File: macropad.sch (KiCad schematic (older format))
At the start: 47 parts, among them P1 USB_C_Plug_USB2.0, SW1 SW_Push, SW10 SW_Push, SW11 Rotary_Encoder_Switch, SW2 SW_Push, SW3 SW_Push, SW4 Rotary_Encoder_Switch, SW5 SW_Push, SW6 SW_Push, SW7 SW_Push, SW8 SW_Push, SW9 SW_Push, U1 ATmega16U2-MU, Y1 16MHz

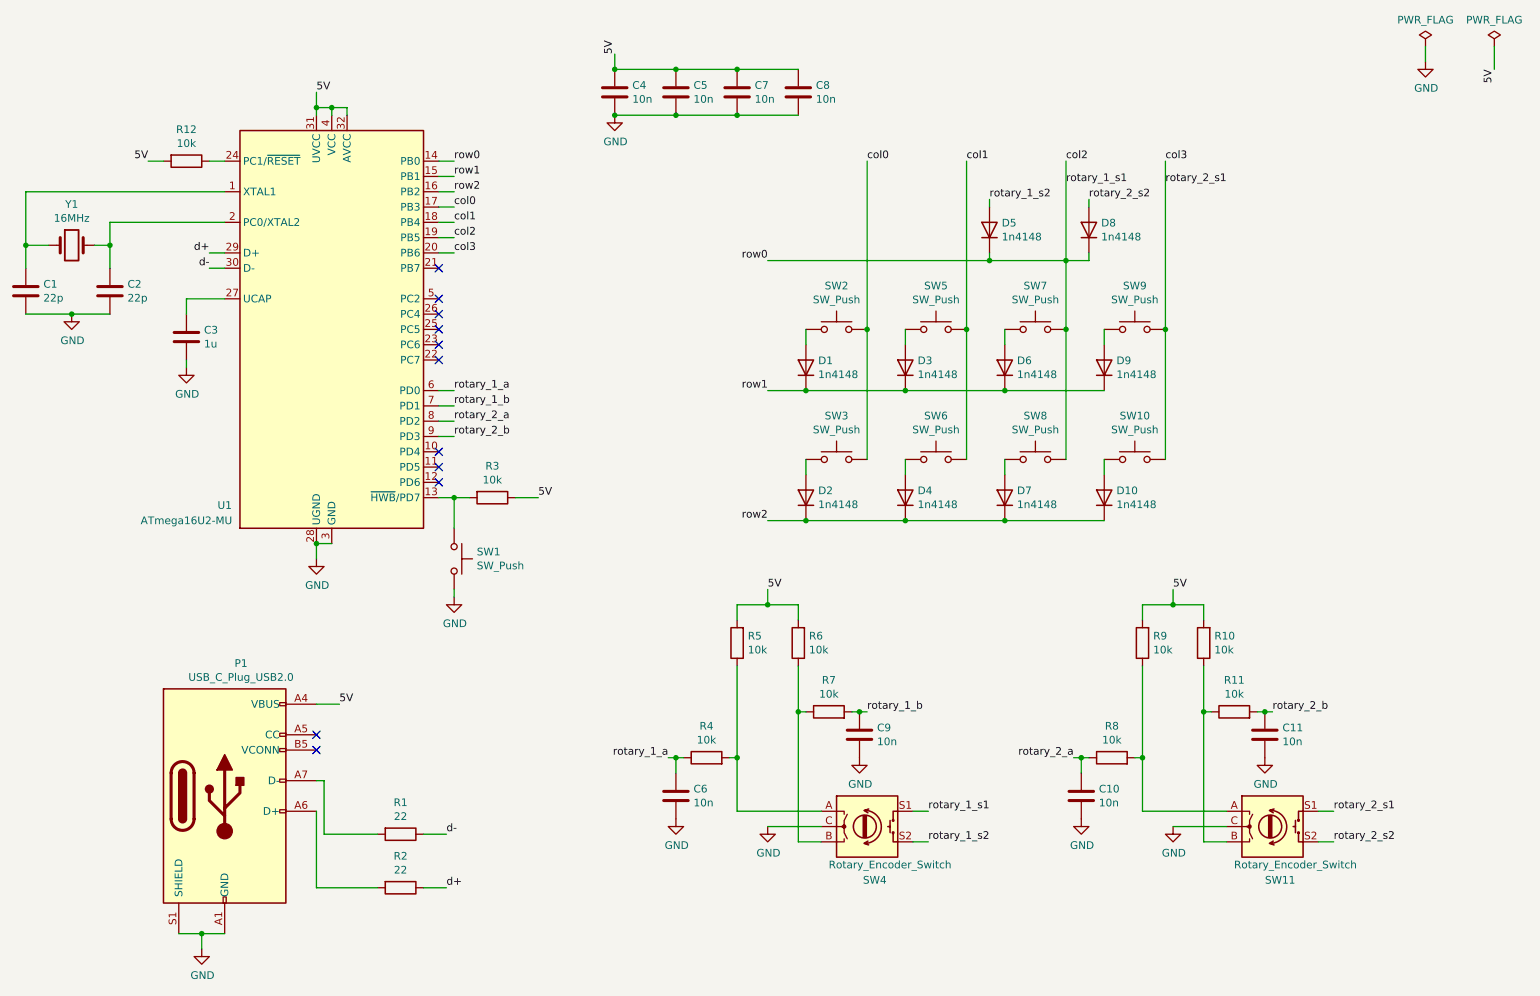
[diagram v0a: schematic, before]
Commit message: use actual models
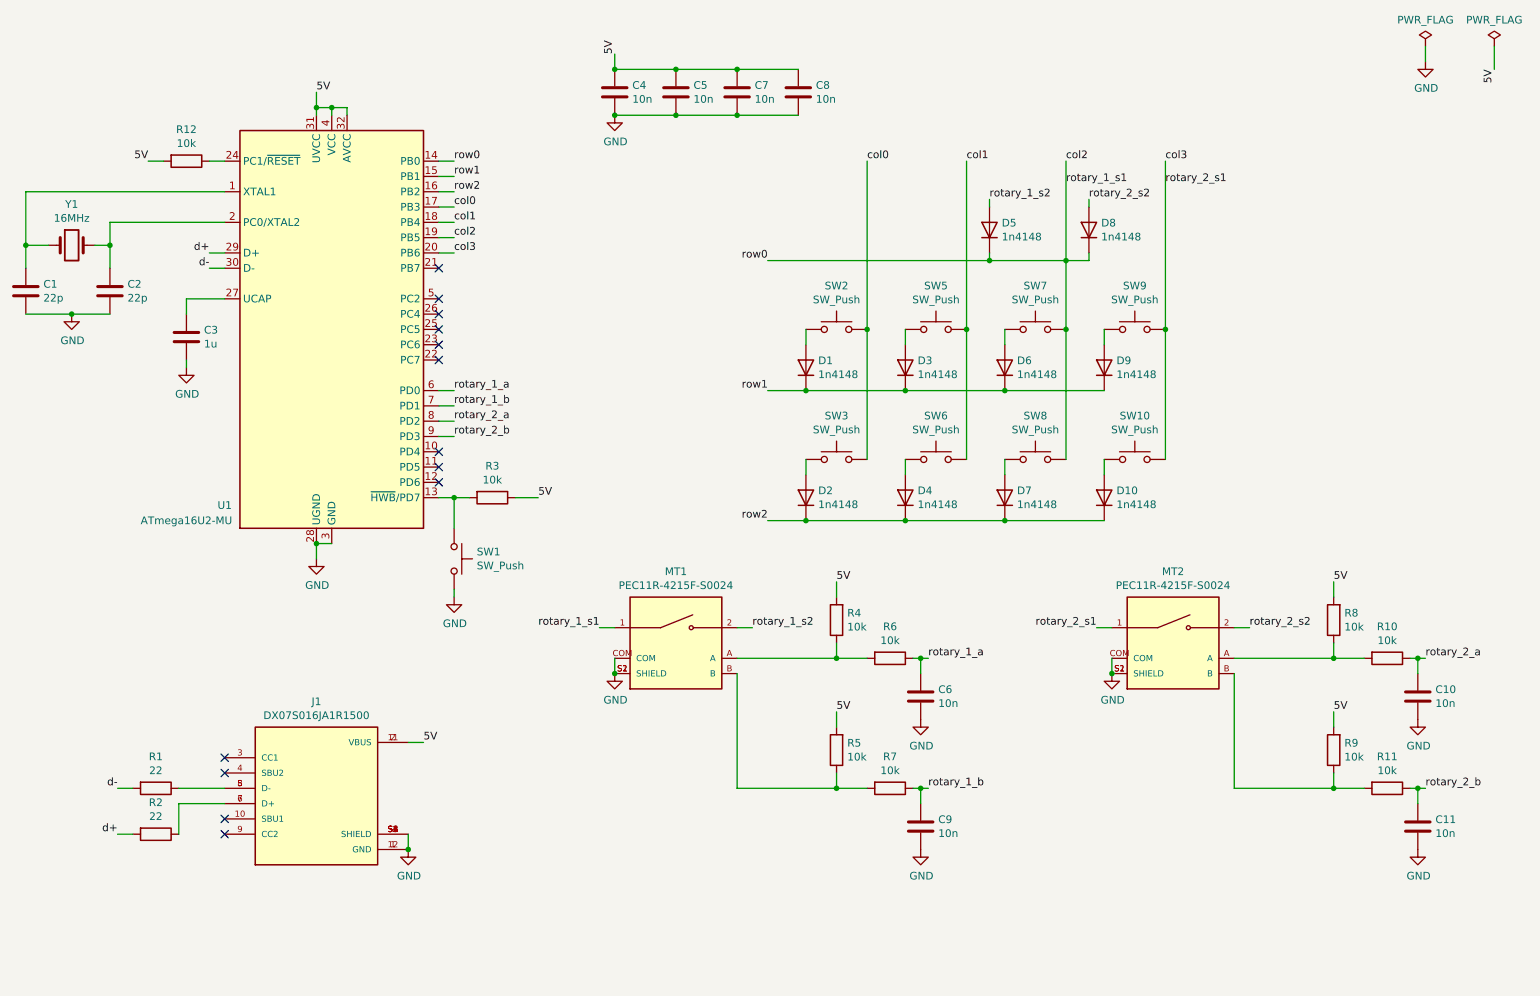
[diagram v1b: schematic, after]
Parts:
- removed P1: USB_C_Plug_USB2.0, DX07S016JA1R1500:JAE_DX07S016JA1R1500, symbol Connector:USB_C_Plug_USB2.0
- removed SW11, SW4: Rotary_Encoder_Switch, PEC11R-4215F-S0024:XDCR_PEC11R-4215F-S0024, symbol Device:Rotary_Encoder_Switch
- added J1: DX07S016JA1R1500, DX07S016JA1R1500:JAE_DX07S016JA1R1500, symbol DX07S016JA1R1500:DX07S016JA1R1500
- added MT1, MT2: PEC11R-4215F-S0024, PEC11R-4215F-S0024:XDCR_PEC11R-4215F-S0024, symbol PEC11R-4215F-S0024:PEC11R-4215F-S0024
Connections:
- net 5V: now also R4.2, R8.2, J1.11 (VBUS), J1.2 (VBUS); no longer R10.2, R6.2
- net GND: now also J1.1 (GND), J1.12 (GND), J1.S1 (SHIELD), J1.S2 (SHIELD), J1.S3 (SHIELD), J1.S4 (SHIELD), J1.S5 (SHIELD), J1.S6 (SHIELD), MT1.COM, MT1.S1 (SHIELD), MT1.S2 (SHIELD), MT2.COM, MT2.S1 (SHIELD), MT2.S2 (SHIELD)
- net col2: now also MT1.1
- net col3: now also MT2.1
- net d+: now also R2.2; no longer R2.1
- net d-: now also R1.2; no longer R1.1
- net rotary_1_a: now also R6.1; no longer R4.1
- net rotary_1_b: now also R7.1; no longer R7.2
- net rotary_1_s2: now also MT1.2
- net rotary_2_a: now also R10.1; no longer R8.1
- net rotary_2_b: now also R11.1; no longer R11.2
- net rotary_2_s2: now also MT2.2
- net at R5.1: now also R7.2, MT1.B; no longer R4.2
- net at R9.1: now also R11.2, MT2.B; no longer R8.2
- new net: J1.5 (D-), J1.8 (D-), R1.1
- new net: J1.6 (D+), J1.7 (D+), R2.1
- new net: MT1.A, R4.1, R6.2
- new net: MT2.A, R10.2, R8.1
- no-connect marks 11 -> 13

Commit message: seems like a good place to leave it for today
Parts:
- removed C8: 10n, Capacitor_SMD:C_0603_1608Metric, symbol Device:C
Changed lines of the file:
@@
-	1    0    0    -1
-$EndComp
-$Comp
-L Device:C C8
-U 1 1 6056B643
-P 6100 1150
-F 0 "C8" H 6215 1196 50  0000 L CNN
-F 1 "10n" H 6215 1105 50  0000 L CNN
-F 2 "Capacitor_SMD:C_0603_1608Metric" H 6138 1000 50  0001 C CNN
-F 3 "~" H 6100 1150 50  0001 C CNN
-	1    6100 1150
 	1    0    0    -1
 $EndComp
@@
 Connection ~ 5300 1300
 Wire Wire Line
-	5700 1300 6100 1300
-Connection ~ 5700 1300
-Wire Wire Line
-	6100 1000 5700 1000
-Wire Wire Line
 	5700 1000 5300 1000
-Connection ~ 5700 1000
 Wire Wire Line
 	4900 1000 5300 1000

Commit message: Fix everything forever
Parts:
- removed Y1: 16MHz, Crystal:Crystal_SMD_3225-4Pin_3.2x2.5mm, symbol Device:Crystal
- added Y1: 16MHz, Crystal:Crystal_SMD_3225-4Pin_3.2x2.5mm, symbol Device:Crystal_GND24
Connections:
- net GND: now also Y1.2, Y1.4
- net at C1.1, U1.1 (XTAL1): now also Y1.1
- net at C2.1, U1.2 (PC0/XTAL2): now also Y1.3
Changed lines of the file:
@@
 	2250 1600 2350 1600
-$Comp
-L Device:Crystal Y1
-U 1 1 60533B4C
-P 1350 2150
-F 0 "Y1" H 1350 2418 50  0000 C CNN
-F 1 "16MHz" H 1350 2327 50  0000 C CNN
-F 2 "Crystal:Crystal_SMD_3225-4Pin_3.2x2.5mm" H 1350 2150 50  0001 C CNN
-F 3 "~" H 1350 2150 50  0001 C CNN
-	1    1350 2150
-	1    0    0    -1
-$EndComp
 $Comp
 L Device:C C1
@@
 	8950 5700 9600 5700
 Connection ~ 9600 5700
+$Comp
+L Device:Crystal_GND24 Y1
+U 1 1 6050F71C
+P 1350 2150
+F 0 "Y1" H 1544 2196 50  0000 L CNN
+F 1 "16MHz" H 1544 2105 50  0000 L CNN
+F 2 "Crystal:Crystal_SMD_3225-4Pin_3.2x2.5mm" H 1350 2150 50  0001 C CNN
+F 3 "~" H 1350 2150 50  0001 C CNN
+	1    1350 2150
+	1    0    0    -1
+$EndComp
+Wire Wire Line
+	1350 2350 1350 2450
+Wire Wire Line
+	1350 1950 1150 1950
+Wire Wire Line
+	1150 1950 1150 2450
+Wire Wire Line
+	1150 2450 1350 2450
+Connection ~ 1350 2450
+Wire Wire Line
+	1350 2450 1350 2600
 $EndSCHEMATC

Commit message: missed a spot
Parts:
- C1, C2: LCSC (none) -> C1653
- C10, C11, C4, C5, C6, C7, C9: LCSC (none) -> C57112
- C3: LCSC (none) -> C15849
- D1, D10, D2, D3, D4, D5, D6, D7, D8, D9: LCSC (none) -> C2128
- R1, R2: LCSC (none) -> C23345
- R10, R11, R12, R3, R4, R5, R6, R7, R8, R9: LCSC (none) -> C25804
- U1: LCSC (none) -> C17317
- Y1: LCSC (none) -> C13738
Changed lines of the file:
@@
 F 2 "Package_DFN_QFN:QFN-32-1EP_5x5mm_P0.5mm_EP3.1x3.1mm" H 3050 2700 50  0001 C CIN
 F 3 "http://ww1.microchip.com/downloads/en/DeviceDoc/doc7799.pdf" H 3050 2700 50  0001 C CNN
+F 4 "C17317" H 3050 2700 50  0001 C CNN "LCSC"
 	1    3050 2700
 	1    0    0    -1
@@
 F 2 "Diode_SMD:D_SOD-323F" H 6150 2950 50  0001 C CNN
 F 3 "~" H 6150 2950 50  0001 C CNN
+F 4 "C2128" V 6150 2950 50  0001 C CNN "LCSC"
 	1    6150 2950
 	0    -1   -1   0
@@
 F 2 "Diode_SMD:D_SOD-323F" H 6800 2950 50  0001 C CNN
 F 3 "~" H 6800 2950 50  0001 C CNN
+F 4 "C2128" V 6800 2950 50  0001 C CNN "LCSC"
 	1    6800 2950
 	0    -1   -1   0
@@
 F 2 "Diode_SMD:D_SOD-323F" H 7450 2950 50  0001 C CNN
 F 3 "~" H 7450 2950 50  0001 C CNN
+F 4 "C2128" V 7450 2950 50  0001 C CNN "LCSC"
 	1    7450 2950
 	0    -1   -1   0
@@
 F 2 "Diode_SMD:D_SOD-323F" H 8100 2950 50  0001 C CNN
 F 3 "~" H 8100 2950 50  0001 C CNN
+F 4 "C2128" V 8100 2950 50  0001 C CNN "LCSC"
 	1    8100 2950
 	0    -1   -1   0
@@
 F 2 "Diode_SMD:D_SOD-323F" H 6150 3800 50  0001 C CNN
 F 3 "~" H 6150 3800 50  0001 C CNN
+F 4 "C2128" V 6150 3800 50  0001 C CNN "LCSC"
 	1    6150 3800
 	0    -1   -1   0
@@
 F 2 "Diode_SMD:D_SOD-323F" H 6800 3800 50  0001 C CNN
 F 3 "~" H 6800 3800 50  0001 C CNN
+F 4 "C2128" V 6800 3800 50  0001 C CNN "LCSC"
 	1    6800 3800
 	0    -1   -1   0
@@
 F 2 "Diode_SMD:D_SOD-323F" H 7450 3800 50  0001 C CNN
 F 3 "~" H 7450 3800 50  0001 C CNN
+F 4 "C2128" V 7450 3800 50  0001 C CNN "LCSC"
 	1    7450 3800
 	0    -1   -1   0
@@
 F 2 "Diode_SMD:D_SOD-323F" H 8100 3800 50  0001 C CNN
 F 3 "~" H 8100 3800 50  0001 C CNN
+F 4 "C2128" V 8100 3800 50  0001 C CNN "LCSC"
 	1    8100 3800
 	0    -1   -1   0
@@
 F 2 "Diode_SMD:D_SOD-323F" H 7350 2050 50  0001 C CNN
 F 3 "~" H 7350 2050 50  0001 C CNN
+F 4 "C2128" V 7350 2050 50  0001 C CNN "LCSC"
 	1    7350 2050
 	0    -1   -1   0
@@
 F 2 "Diode_SMD:D_SOD-323F" H 8000 2050 50  0001 C CNN
 F 3 "~" H 8000 2050 50  0001 C CNN
+F 4 "C2128" V 8000 2050 50  0001 C CNN "LCSC"
 	1    8000 2050
 	0    -1   -1   0
@@
 F 2 "Capacitor_SMD:C_0603_1608Metric" H 2138 2600 50  0001 C CNN
 F 3 "~" H 2100 2750 50  0001 C CNN
+F 4 "C15849" H 2100 2750 50  0001 C CNN "LCSC"
 	1    2100 2750
 	1    0    0    -1
@@
 F 2 "Capacitor_SMD:C_0603_1608Metric" H 1088 2300 50  0001 C CNN
 F 3 "~" H 1050 2450 50  0001 C CNN
+F 4 "C1653" H 1050 2450 50  0001 C CNN "LCSC"
 	1    1050 2450
 	1    0    0    -1
@@
 F 2 "Capacitor_SMD:C_0603_1608Metric" H 1638 2300 50  0001 C CNN
 F 3 "~" H 1600 2450 50  0001 C CNN
+F 4 "C1653" H 1600 2450 50  0001 C CNN "LCSC"
 	1    1600 2450
 	1    0    0    -1
@@
 F 2 "Capacitor_SMD:C_0603_1608Metric" H 4938 1000 50  0001 C CNN
 F 3 "~" H 4900 1150 50  0001 C CNN
+F 4 "C57112" H 4900 1150 50  0001 C CNN "LCSC"
 	1    4900 1150
 	1    0    0    -1
@@
 F 2 "Capacitor_SMD:C_0603_1608Metric" H 5338 1000 50  0001 C CNN
 F 3 "~" H 5300 1150 50  0001 C CNN
+F 4 "C57112" H 5300 1150 50  0001 C CNN "LCSC"
 	1    5300 1150
 	1    0    0    -1
@@
 F 2 "Capacitor_SMD:C_0603_1608Metric" H 5738 1000 50  0001 C CNN
 F 3 "~" H 5700 1150 50  0001 C CNN
+F 4 "C57112" H 5700 1150 50  0001 C CNN "LCSC"
 	1    5700 1150
 	1    0    0    -1
@@
 F 2 "Resistor_SMD:R_0603_1608Metric" V 4030 3800 50  0001 C CNN
 F 3 "~" H 4100 3800 50  0001 C CNN
+F 4 "C25804" V 4100 3800 50  0001 C CNN "LCSC"
 	1    4100 3800
 	0    1    1    0
@@
 F 2 "Resistor_SMD:R_0603_1608Metric" V 2030 1600 50  0001 C CNN
 F 3 "~" H 2100 1600 50  0001 C CNN
+F 4 "C25804" V 2100 1600 50  0001 C CNN "LCSC"
 	1    2100 1600
 	0    1    1    0
@@
 F 2 "Resistor_SMD:R_0603_1608Metric" V 1830 5700 50  0001 C CNN
 F 3 "~" H 1900 5700 50  0001 C CNN
+F 4 "C23345" V 1900 5700 50  0001 C CNN "LCSC"
 	1    1900 5700
 	0    1    1    0
@@
 F 2 "Resistor_SMD:R_0603_1608Metric" V 1830 6000 50  0001 C CNN
 F 3 "~" H 1900 6000 50  0001 C CNN
+F 4 "C23345" V 1900 6000 50  0001 C CNN "LCSC"
 	1    1900 6000
 	0    1    1    0
@@
 F 2 "Resistor_SMD:R_0603_1608Metric" V 6630 4850 50  0001 C CNN
 F 3 "~" H 6700 4850 50  0001 C CNN
+F 4 "C25804" V 6700 4850 50  0001 C CNN "LCSC"
 	1    6700 4850
 	0    1    1    0
@@
 F 2 "Capacitor_SMD:C_0603_1608Metric" H 6938 4950 50  0001 C CNN
 F 3 "~" H 6900 5100 50  0001 C CNN
+F 4 "C57112" H 6900 5100 50  0001 C CNN "LCSC"
 	1    6900 5100
 	1    0    0    -1
@@
 F 2 "Resistor_SMD:R_0603_1608Metric" V 6280 4600 50  0001 C CNN
 F 3 "~" H 6350 4600 50  0001 C CNN
+F 4 "C25804" H 6350 4600 50  0001 C CNN "LCSC"
 	1    6350 4600
 	-1   0    0    1
@@
 F 2 "Resistor_SMD:R_0603_1608Metric" V 6630 5700 50  0001 C CNN
 F 3 "~" H 6700 5700 50  0001 C CNN
+F 4 "C25804" V 6700 5700 50  0001 C CNN "LCSC"
 	1    6700 5700
 	0    1    1    0
@@
 F 2 "Capacitor_SMD:C_0603_1608Metric" H 6938 5800 50  0001 C CNN
 F 3 "~" H 6900 5950 50  0001 C CNN
+F 4 "C57112" H 6900 5950 50  0001 C CNN "LCSC"
 	1    6900 5950
 	1    0    0    -1
@@
 F 2 "Resistor_SMD:R_0603_1608Metric" V 6280 5450 50  0001 C CNN
 F 3 "~" H 6350 5450 50  0001 C CNN
+F 4 "C25804" H 6350 5450 50  0001 C CNN "LCSC"
 	1    6350 5450
 	-1   0    0    1
@@
 F 2 "Resistor_SMD:R_0603_1608Metric" V 9880 4850 50  0001 C CNN
 F 3 "~" H 9950 4850 50  0001 C CNN
+F 4 "C25804" V 9950 4850 50  0001 C CNN "LCSC"
 	1    9950 4850
 	0    1    1    0
@@
 F 2 "Capacitor_SMD:C_0603_1608Metric" H 10188 4950 50  0001 C CNN
 F 3 "~" H 10150 5100 50  0001 C CNN
+F 4 "C57112" H 10150 5100 50  0001 C CNN "LCSC"
 	1    10150 5100
 	1    0    0    -1
@@
 F 2 "Resistor_SMD:R_0603_1608Metric" V 9530 4600 50  0001 C CNN
 F 3 "~" H 9600 4600 50  0001 C CNN
+F 4 "C25804" H 9600 4600 50  0001 C CNN "LCSC"
 	1    9600 4600
 	-1   0    0    1
@@
 F 2 "Resistor_SMD:R_0603_1608Metric" V 9880 5700 50  0001 C CNN
 F 3 "~" H 9950 5700 50  0001 C CNN
+F 4 "C25804" V 9950 5700 50  0001 C CNN "LCSC"
 	1    9950 5700
 	0    1    1    0
@@
 F 2 "Capacitor_SMD:C_0603_1608Metric" H 10188 5800 50  0001 C CNN
 F 3 "~" H 10150 5950 50  0001 C CNN
+F 4 "C57112" H 10150 5950 50  0001 C CNN "LCSC"
 	1    10150 5950
 	1    0    0    -1
@@
 F 2 "Resistor_SMD:R_0603_1608Metric" V 9530 5450 50  0001 C CNN
 F 3 "~" H 9600 5450 50  0001 C CNN
+F 4 "C25804" H 9600 5450 50  0001 C CNN "LCSC"
 	1    9600 5450
 	-1   0    0    1
@@
 F 2 "Crystal:Crystal_SMD_3225-4Pin_3.2x2.5mm" H 1350 2150 50  0001 C CNN
 F 3 "~" H 1350 2150 50  0001 C CNN
+F 4 "C13738" H 1350 2150 50  0001 C CNN "LCSC"
 	1    1350 2150
 	1    0    0    -1

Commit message: Fix bugs discovered in first board
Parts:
- removed SW1: SW_Push, 1825910-7:SW_1825910-7, symbol Switch:SW_Push
- added R13, R14: 5.1k, Resistor_SMD:R_0603_1608Metric, symbol Device:R
- added TP1: ~RESET, TestPoint:TestPoint_Pad_D1.0mm, symbol Connector:TestPoint
- added TP2: ~HWB, TestPoint:TestPoint_Pad_D1.0mm, symbol Connector:TestPoint
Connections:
- net GND: now also R13.2, R14.1
- net col2: no longer D5.1 (K), D8.1 (K), U1.14 (PB0)
- net at R3.2, U1.13 (~HWB~/PD7): now also TP2.1
- net at R12.1, U1.24 (PC1/~RESET): now also TP1.1
- net at J1.3 (CC1): now also R14.2
- net at J1.9 (CC2): now also R13.1
- new net row0: D5.1 (K), D8.1 (K), U1.14 (PB0)
- no-connect marks 13 -> 11
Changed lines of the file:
@@
 Text Label 7850 1600 0    50   ~ 0
 col2
-Wire Wire Line
-	7850 1600 7850 2250
 Connection ~ 7850 2700
 Text Label 8500 1600 0    50   ~ 0
@@
 	0    -1   -1   0
 $EndComp
-Connection ~ 7850 2250
-Wire Wire Line
-	7850 2250 7850 2700
 Text Label 5900 2250 2    50   ~ 0
 row0
@@
 Wire Wire Line
 	7350 2200 7350 2250
-Connection ~ 7350 2250
-Wire Wire Line
-	7350 2250 7850 2250
 Wire Wire Line
 	7350 1850 7350 1900
@@
 Wire Wire Line
 	8000 2200 8000 2250
-Wire Wire Line
-	8000 2250 7850 2250
 $Comp
 L Device:C C3
@@
 5V
 Wire Wire Line
-	2250 1600 2350 1600
+	2250 1600 2300 1600
 $Comp
 L Device:C C1
@@
 $EndComp
 Connection ~ 4900 1300
-$Comp
-L Switch:SW_Push SW1
-U 1 1 60590D31
-P 3850 4200
-F 0 "SW1" V 3804 4348 50  0000 L CNN
-F 1 "SW_Push" V 3895 4348 50  0000 L CNN
-F 2 "1825910-7:SW_1825910-7" H 3850 4400 50  0001 C CNN
-F 3 "~" H 3850 4400 50  0001 C CNN
-	1    3850 4200
-	0    1    1    0
-$EndComp
 Text Label 4400 3800 0    50   ~ 0
 5V
@@
 $EndComp
 Wire Wire Line
-	3750 3800 3850 3800
-Wire Wire Line
 	4400 3800 4250 3800
-Wire Wire Line
-	3850 4000 3850 3800
-Connection ~ 3850 3800
-Wire Wire Line
-	3850 3800 3950 3800
-$Comp
-L power:GND #PWR05
-U 1 1 605B8194
-P 3850 4450
-F 0 "#PWR05" H 3850 4200 50  0001 C CNN
-F 1 "GND" H 3855 4277 50  0000 C CNN
-F 2 "" H 3850 4450 50  0001 C CNN
-F 3 "" H 3850 4450 50  0001 C CNN
-	1    3850 4450
-	1    0    0    -1
-$EndComp
-Wire Wire Line
-	3850 4450 3850 4400
 NoConn ~ 3750 2500
 NoConn ~ 3750 2600
@@
 Wire Wire Line
 	1650 6000 1750 6000
-NoConn ~ 2350 5500
 NoConn ~ 2350 5600
 NoConn ~ 2350 5900
-NoConn ~ 2350 6000
 Wire Wire Line
 	3550 6000 3550 6100
@@
 Wire Wire Line
 	1350 2450 1350 2600
+Wire Wire Line
+	7850 1600 7850 2700
+Wire Wire Line
+	8000 2250 7350 2250
+Connection ~ 7350 2250
+Wire Wire Line
+	3750 3800 3850 3800
+$Comp
+L Device:R R14
+U 1 1 605B4566
+P 2250 5200
+F 0 "R14" H 2320 5246 50  0000 L CNN
+F 1 "5.1k" H 2320 5155 50  0000 L CNN
+F 2 "Resistor_SMD:R_0603_1608Metric" V 2180 5200 50  0001 C CNN
+F 3 "~" H 2250 5200 50  0001 C CNN
+F 4 " C23186" H 2250 5200 50  0001 C CNN "LCSC"
+	1    2250 5200
+	1    0    0    -1
+$EndComp
+Wire Wire Line
+	2350 5500 2250 5500
+Wire Wire Line
+	2250 5500 2250 5350
+$Comp
+L Device:R R13
+U 1 1 605B96D1
+P 2200 6250
+F 0 "R13" H 2270 6296 50  0000 L CNN
+F 1 "5.1k" H 2270 6205 50  0000 L CNN
+F 2 "Resistor_SMD:R_0603_1608Metric" V 2130 6250 50  0001 C CNN
+F 3 "~" H 2200 6250 50  0001 C CNN
+F 4 " C23186" H 2200 6250 50  0001 C CNN "LCSC"
+	1    2200 6250
+	1    0    0    -1
+$EndComp
+Wire Wire Line
+	2350 6000 2200 6000
+Wire Wire Line
+	2200 6000 2200 6100
+$Comp
+L power:GND #PWR014
+U 1 1 605BEE86
+P 2200 6450
+F 0 "#PWR014" H 2200 6200 50  0001 C CNN
+F 1 "GND" H 2205 6277 50  0000 C CNN
+F 2 "" H 2200 6450 50  0001 C CNN
+F 3 "" H 2200 6450 50  0001 C CNN
+	1    2200 6450
+	1    0    0    -1
+$EndComp
+Wire Wire Line
+	2200 6450 2200 6400
+$Comp
+L power:GND #PWR05
+U 1 1 605C3CA8
+P 2050 5100
+F 0 "#PWR05" H 2050 4850 50  0001 C CNN
+F 1 "GND" H 2055 4927 50  0000 C CNN
+F 2 "" H 2050 5100 50  0001 C CNN
+F 3 "" H 2050 5100 50  0001 C CNN
+	1    2050 5100
+	1    0    0    -1
+$EndComp
+Wire Wire Line
+	2050 5100 2050 5050
+Wire Wire Line
+	2050 5050 2250 5050
+$Comp
+L Connector:TestPoint TP2
+U 1 1 605CA1C1
+P 3850 3950
+F 0 "TP2" H 3792 3970 50  0000 R CNN
+F 1 "~HWB" H 3792 4068 50  0000 R CNN
+F 2 "TestPoint:TestPoint_Pad_D1.0mm" H 4050 3950 50  0001 C CNN
+F 3 "~" H 4050 3950 50  0001 C CNN
+	1    3850 3950
+	-1   0    0    1
+$EndComp
+Wire Wire Line
+	3850 3950 3850 3800
+Connection ~ 3850 3800
+Wire Wire Line
+	3850 3800 3950 3800
+$Comp
+L Connector:TestPoint TP1
+U 1 1 605D4EEA
+P 2300 1250
+F 0 "TP1" H 2358 1374 50  0000 L CNN
+F 1 "~RESET" H 2358 1276 50  0000 L CNN
+F 2 "TestPoint:TestPoint_Pad_D1.0mm" H 2500 1250 50  0001 C CNN
+F 3 "~" H 2500 1250 50  0001 C CNN
+	1    2300 1250
+	1    0    0    -1
+$EndComp
+Wire Wire Line
+	2300 1250 2300 1600
+Connection ~ 2300 1600
+Wire Wire Line
+	2300 1600 2350 1600
 $EndSCHEMATC
